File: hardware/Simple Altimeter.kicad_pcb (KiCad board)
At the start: 4 copper layers, 14.7 x 27.7 mm, 33 parts, among them J1 USB_C_Receptacle_USB2.0, J2 Conn_01x05_Pin, J3 Conn_01x02_Pin, SW1 SW_Push, U2 BMP280, U3 W25Q16JVUXIQ, U4 STM32F042G6Ux, U7 STNS01

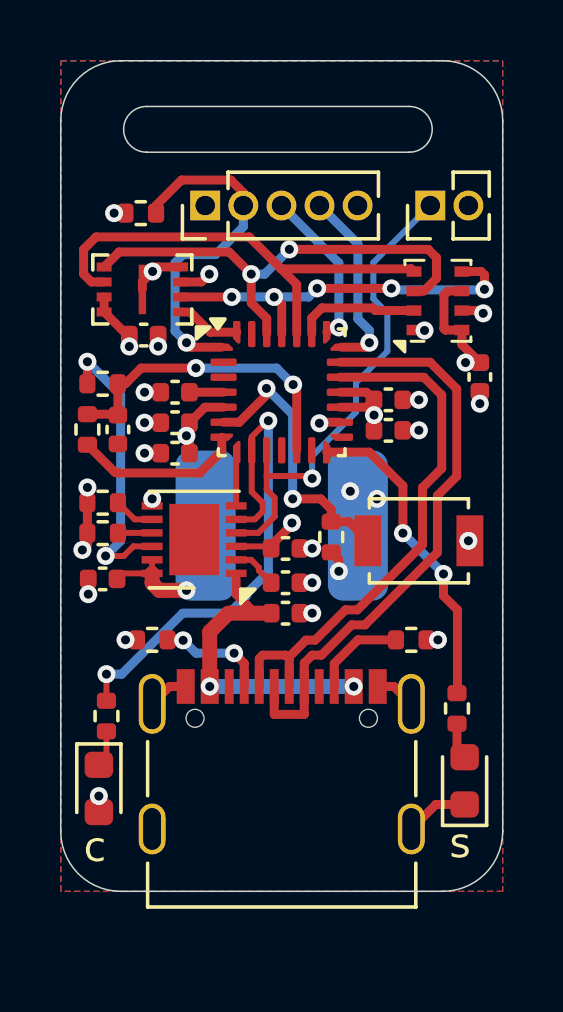
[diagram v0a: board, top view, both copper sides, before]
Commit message: Hardware improvements including a smaller PCB, buzzer and updated file formats to Kicad 8.
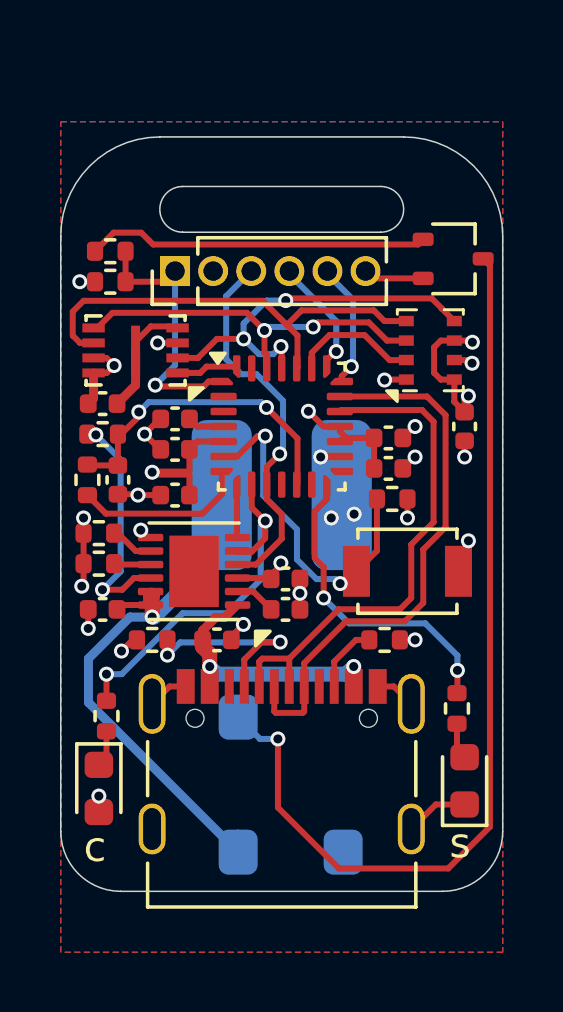
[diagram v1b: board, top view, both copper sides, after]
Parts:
- removed J3: Conn_01x02_Pin, Connector_PinHeader_1.27mm:PinHeader_1x02_P1.27mm_Vertical
- added BZ1: Buzzer, My Footprints:Buzzer_0502, B.Cu at (149.5, 122.7)
- added Q1: BC847W, Package_TO_SOT_SMD:SOT-323_SC-70, F.Cu at (155.1, 105.2)
- added R9: 1k, Resistor_SMD:R_0402_1005Metric, F.Cu at (143.6, 104.9)
- BT1: footprint Footprints:Lipo 401010 -> My Footprints:Lipo 401010
- J2: value Conn_01x05_Pin -> Conn_01x06_Pin; footprint Connector_PinHeader_1.27mm:PinHeader_1x05_P1.27mm_Vertical -> Connector_PinHeader_1.27mm:PinHeader_1x06_P1.27mm_Vertical
- U3: footprint Footprints:Winbond_USON_8_EP_2x3mm -> My Footprints:Winbond_USON_8_EP_2x3mm
- U7: footprint Package_DFN_QFN:DFN-12-1EP_3x3mm_P0.45mm_EP1.66x2.38mm -> Package_DFN_QFN:DFN-12-1EP_3x3mm_P0.45mm_EP1.65x2.38mm
- moved C13 2.66 mm to (143.4, 110.0)
- moved R14 2.50 mm to (143.6, 105.9)
- moved C7 2.45 mm to (147.2, 117.9)
- moved J2 2.40 mm to (145.8, 105.6)
- moved R6 2.40 mm to (153.0, 113.2), turned to 0 degrees
- moved U3 2.04 mm to (144.5, 108.2)
- moved C5 1.73 mm to (155.4, 110.7)
- moved C4 1.68 mm to (143.9, 112.5)
- moved R1 1.68 mm to (143.4, 111.0)
- moved R2 1.68 mm to (142.9, 112.5)
- moved U2 1.67 mm to (154.3, 108.2)
- moved C10 1.40 mm to (145.8, 113.0)
- moved C6 1.27 mm to (152.9, 112.1)
- moved C8 1.27 mm to (152.9, 111.1)
- moved U4 1.14 mm to (149.4, 110.7)
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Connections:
- net Net-(BT1-+) renamed VBAT
- J2 pad 1: +3.3V -> /BUZZER/BOOT
- J2 pad 2: /BOOT -> +3.3V
- J2 pad 3: /SWDCLK -> /SHUTDOWN
- J2 pad 4: /SWDIO -> /SWDCLK
- J2 pad 5: GND -> /SWDIO
- R14 pad 1: /BOOT -> /BUZZER/BOOT
- U4 pad 1: /BOOT -> /BUZZER/BOOT
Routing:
- net Net-(BZ1--): track 0.00 -> 31.4 mm, vias 0 -> 1
- net VBAT: track 3.27 -> 19.1 mm
- net /BOOT: track 11.7 -> 0.00 mm, vias 1 -> 0
- net Net-(Q1-B): track 0.00 -> 11.4 mm
- net /BUZZER/BOOT: track 0.00 -> 9.19 mm, vias 0 -> 1
- net GND: track 17.8 -> 25.3 mm, vias 24 -> 20
- net /~{CHARGE}: track 17.2 -> 12.5 mm
- net +3.3V: track 15.8 -> 20.1 mm, vias 8 -> 9
- net /SHUTDOWN: track 16.5 -> 12.7 mm
- net /MOSI: track 15.9 -> 12.4 mm
- net Net-(J1-CC1): track 3.65 -> 6.78 mm
- net +5V: track 11.1 -> 8.57 mm
- net /BUTTON: track 9.40 -> 11.5 mm
- net /SWDIO: track 6.25 -> 4.19 mm
- net Net-(U7-BATMS): track 9.55 -> 7.86 mm
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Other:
- board size 14.7 x 27.7 mm -> 14.7 x 25.1 mm
- board text added: "SimpleAlt Rev3"
- board text removed: "(C) 2024 Michael Turner"
- board text removed: "SimpleAlt Rev2"
